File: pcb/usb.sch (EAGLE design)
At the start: 23 parts, among them CN2 JSTPH, Q1 mmbt2222, Q2 mmbt2222, Q3 DMG3415U, U2 MIC5225-3.3v, U4 CH340G, U6 MCP73831T-2ACI/OT

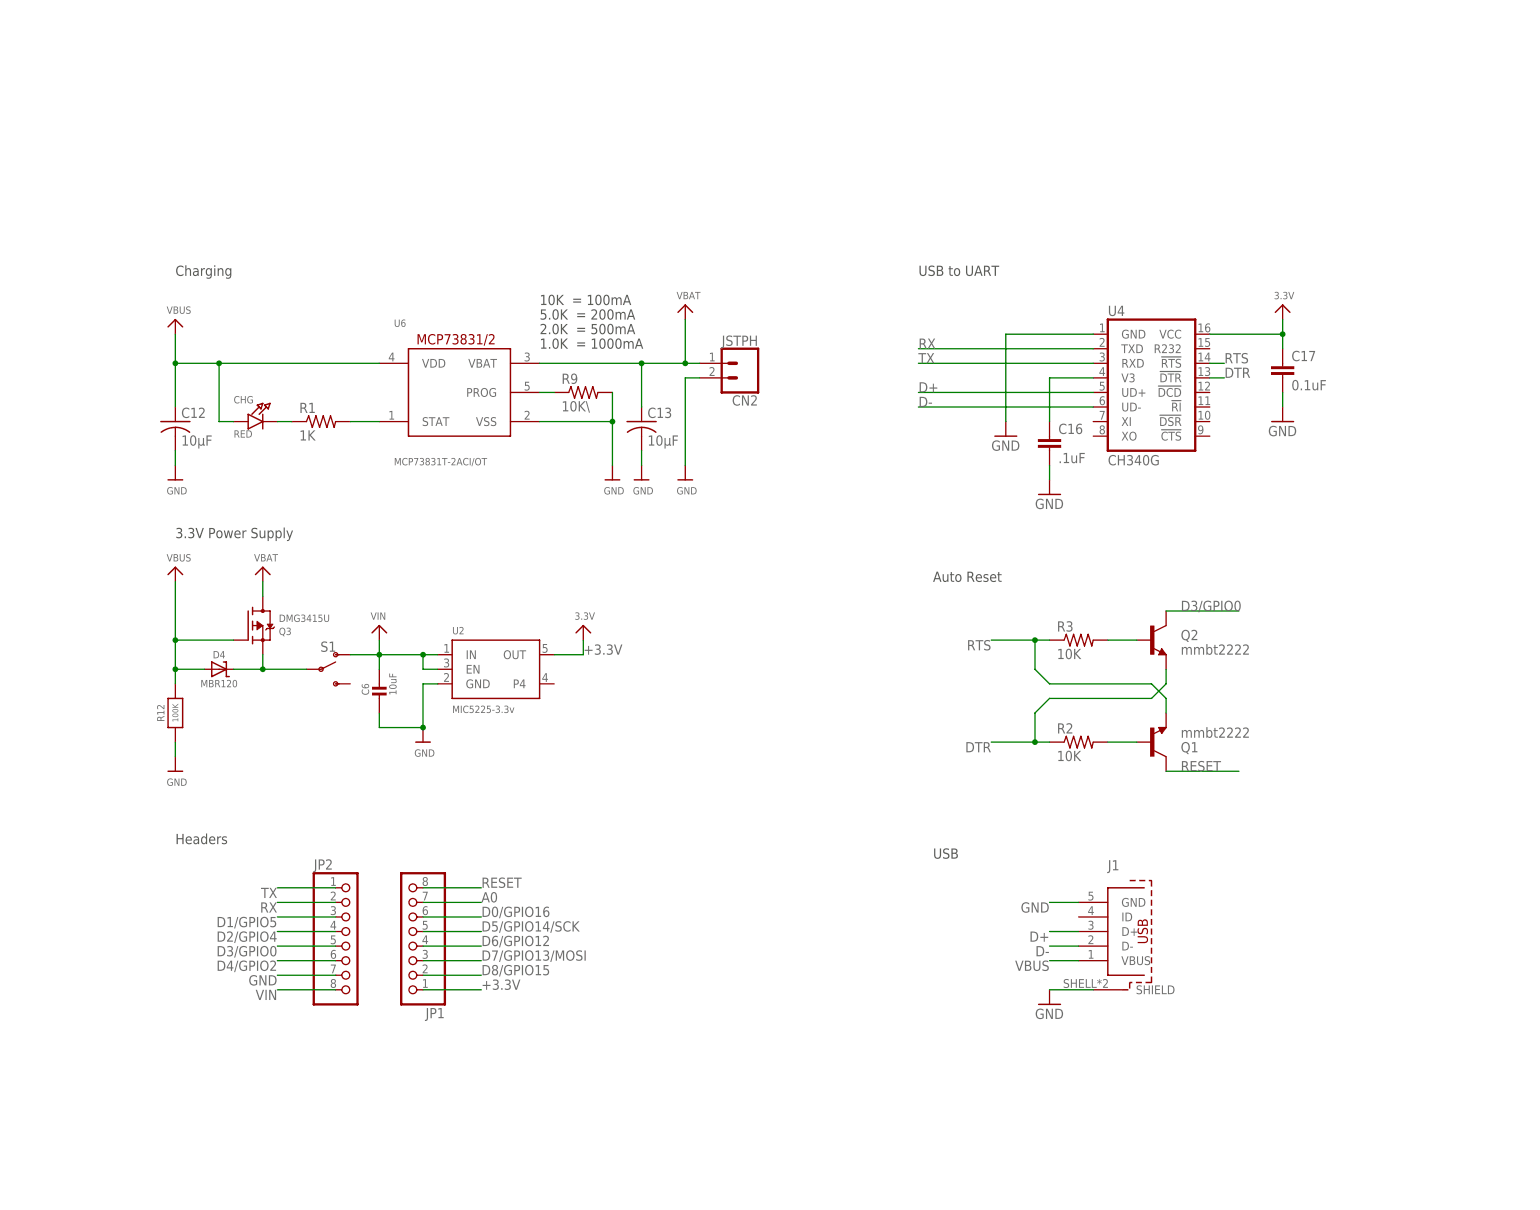
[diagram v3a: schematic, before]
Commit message: V2 usb board ordered
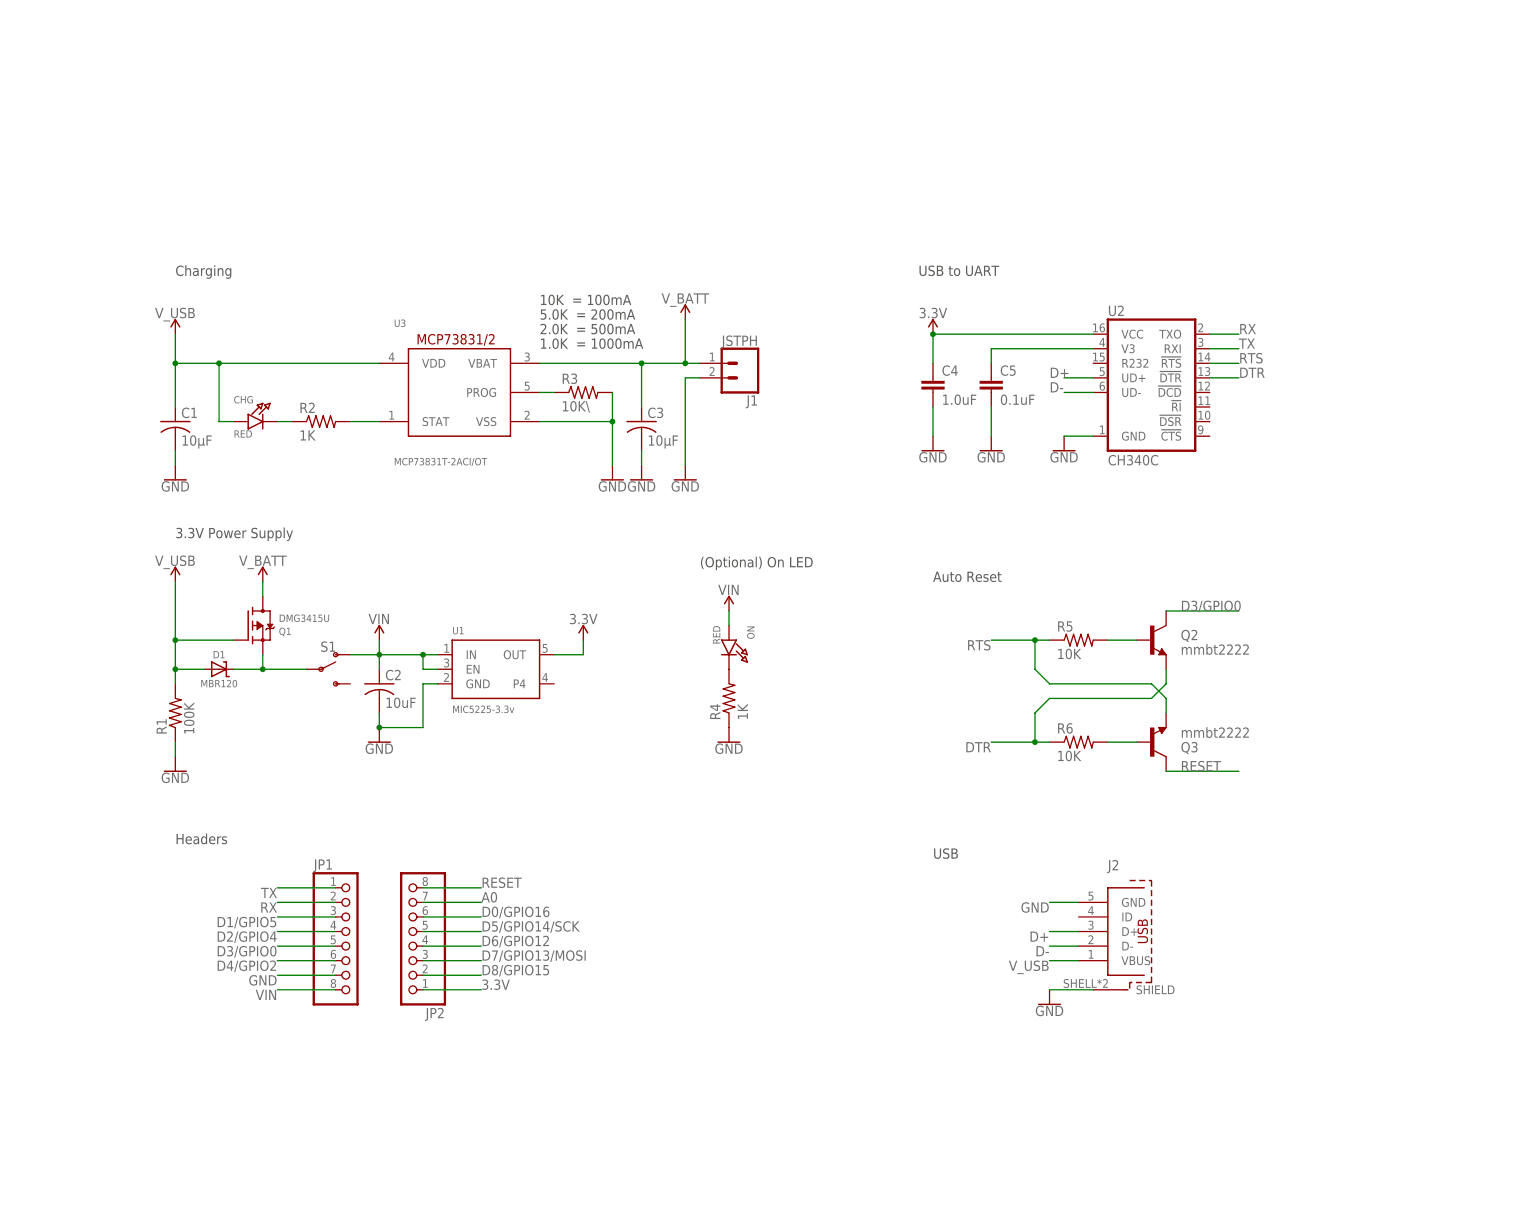
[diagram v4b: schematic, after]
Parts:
- removed C16: .1uF, SparkFun-Capacitors:10NF/10000PF-50V-10%(0603)
- removed C17: 0.1uF, SparkFun-Capacitors:0.1UF-25V(+80/-20%)(0603)
- removed C6: 10uF, microbuilder:CAP_CERAMIC0805
- removed CN2: JSTPH, SparkFun-Connectors:CONN_02
- removed R12: 100K, microbuilder:RESISTOR_0603_NOOUT
- removed R9: 10K\, adafruit:R-US_R0805
- removed U4: CH340G, SparkFun-DigitalIC:CH340GSMD
- added C2: 10uF, adafruit:C-USC0805
- added C4: 1.0uF, SparkFun-Capacitors:1.0UF-0805-25V-10%
- added C5: 0.1uF, SparkFun-Capacitors:1.0UF-0805-25V-10%
- added J2: (no value), Wurth_Elektronik_Electromechanic_Input-Output_Connectors_rev19b:614105150621
- added ON: RED, microbuilder:LED0805_NOOUTLINE
- added R4: 1K, adafruit:R-US_R0805
- added R5, R6: 10K, adafruit:R-US_R0603
- added U1: MIC5225-3.3v, microbuilder:VREG_SOT23-5
- J1: value (none) -> JSTPH; device Wurth_Elektronik_Electromechanic_Input-Output_Connectors_rev19a:614105150621 -> SparkFun-Connectors:CONN_02
- Q1: value mmbt2222 -> DMG3415U; device SparkFun:TRANSISTOR_NPNSOT23-3 -> microbuilder:MOSFET-P
- Q3: value DMG3415U -> mmbt2222; device microbuilder:MOSFET-P -> SparkFun:TRANSISTOR_NPNSOT23-3
- R1: value 1K -> 100K
- R2: value 10K -> 1K; device adafruit:R-US_R0603 -> adafruit:R-US_R0805
- R3: value 10K -> 10K\; device adafruit:R-US_R0603 -> adafruit:R-US_R0805
- U2: value MIC5225-3.3v -> CH340C; device microbuilder:VREG_SOT23-5 -> SparkFun-IC-Comms:CH340C
- renumbered C12 to C1, C13 to C3, D4 to D1, U6 to U3
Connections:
- removed net +3.3V: JP1.1, U2.OUT
- removed net V3: C16.1, U4.V3
- removed net VBAT: C3.1, CN2.1, Q3.D, U3.VBAT
- removed net VBUS: C1.1, CHG.A, D1.A, J1.VBUS, Q3.G, R12.2, U3.VDD
- new net N$2: C5.1, U2.V3
- new net N$3: ON.C, R4.2
- new net V_BATT: C3.1, J1.1, Q1.D, U3.VBAT
- new net V_USB: C1.1, CHG.A, D1.A, J2.VBUS, Q1.G, R1.2, U3.VDD
- net 3.3V: now also C4.1, JP2.1, U1.OUT, U2.VCC; no longer C17.1, U4.VCC
- net A0: now also JP2.7; no longer JP1.7
- net D+: now also J2.D+, U2.UD+; no longer J1.D+, U4.UD+
- net D-: now also J2.D-, U2.UD-; no longer J1.D-, U4.UD-
- net D0/GPIO16: now also JP2.6; no longer JP1.6
- net D1/GPIO5: now also JP1.3; no longer JP2.3
- net D2/GPIO4: now also JP1.4; no longer JP2.4
- net D3/GPIO0: now also JP1.5; no longer JP2.5
- net D4/GPIO2: now also JP1.6; no longer JP2.6
- net D5/GPIO14/SCK: now also JP2.5; no longer JP1.5
- net D6/GPIO12: now also JP2.4; no longer JP1.4
- net D7/GPIO13/MOSI: now also JP2.3; no longer JP1.3
- net D8/GPIO15: now also JP2.2; no longer JP1.2
- net DTR: now also R6.1, U2.!DTR; no longer R2.1, U4.!DTR
- net GND: now also C2.2, C4.2, C5.2, J1.2, J2.GND, J2.SHIELD, JP1.7, R1.1, R3.2, R4.1, U1.GND; no longer C16.2, C17.2, C6.P$2, CN2.2, J1.GND, J1.SHIELD, JP2.7, R12.1, R9.2, U4.GND
- net N$1: now also R2.1; no longer R1.1
- net N$13: now also Q3.B, R6.2; no longer Q1.B, R2.2
- net N$14: now also R5.2; no longer R3.2
- net N$4: now also R2.2; no longer R1.2
- net N$7: now also Q1.S; no longer Q3.S
- net N$9: now also R3.1; no longer R9.1
- net RESET: now also JP2.8, Q3.C; no longer JP1.8, Q1.C
- net RTS: now also Q3.E, R5.1, U2.!RTS; no longer Q1.E, R3.1, U4.!RTS
- net RX: now also JP1.2, U2.TXO; no longer JP2.2, U4.TXD
- net TX: now also JP1.1, U2.RXI; no longer JP2.1, U4.RXD
- net VIN: now also C2.1, JP1.8, ON.A, U1.EN, U1.IN; no longer C6.P$1, JP2.8, U2.EN, U2.IN
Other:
- note added: "(Optional) On LED"
- moved on the sheet: JP1, JP2, R1, R2, R3

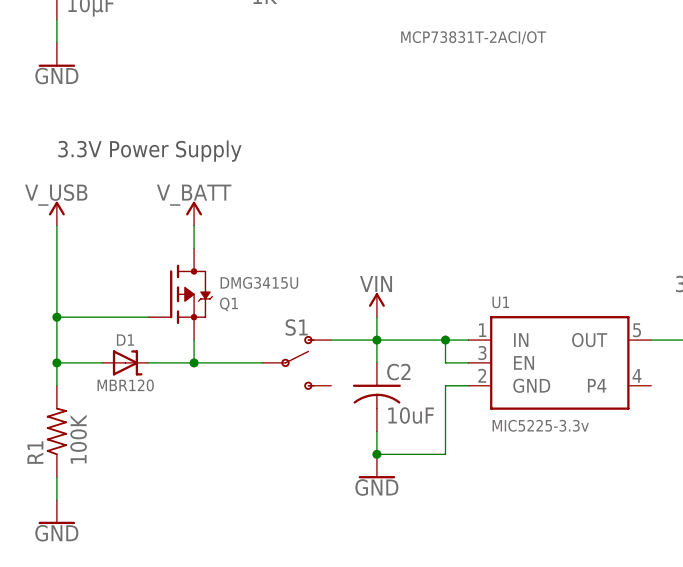
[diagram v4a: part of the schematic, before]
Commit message: Add manufacturer part numbers to USB board
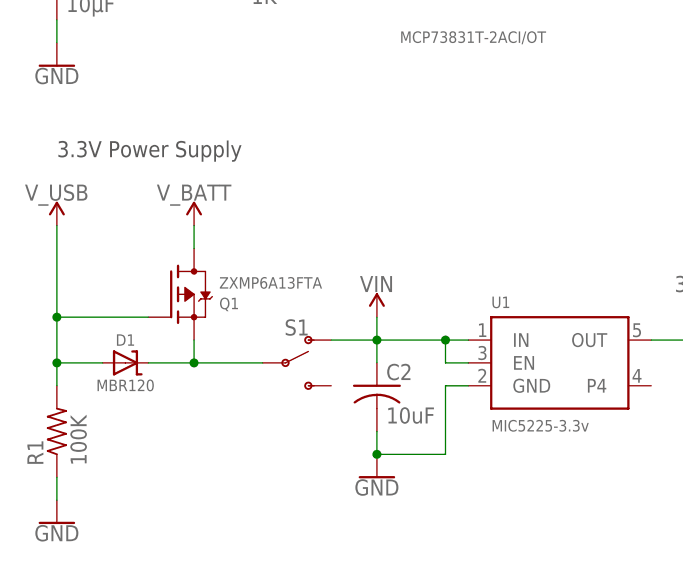
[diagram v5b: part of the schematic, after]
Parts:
- C1, C2, C3: MPN (none) -> EMK212ABJ106KG-T
- C4: MPN (none) -> C0805C105K4RAC7210
- C5: MPN (none) -> 08051C104J4T4A
- CHG: MPN (none) -> SMLD12E3N1WT86
- D1: MPN (none) -> MBR120ESFT1G
- J2: MPN (none) -> 614105150621
- ON: MPN (none) -> SMLEN3WBC8W1
- Q1: value DMG3415U -> ZXMP6A13FTA; MPN (none) -> ZXMP6A13FTA
- Q2, Q3: MPN (none) -> MMBT2222A-G
- R1: MPN (none) -> CR0805AFX-1003EAS
- R2, R4: MPN (none) -> ESR10EZPJ102
- R3, R5, R6: MPN (none) -> CRCW080510K0FKEAC
- S1: MPN (none) -> AYZ0202AGRLC
- U1: MPN (none) -> MIC5225-3.3YM5-TR
- U2: MPN (none) -> CH340C
- U3: MPN (none) -> MCP73831T-2ACI/OT

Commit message: Add part numbers for the headers on the usb board
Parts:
- JP1, JP2: MPN (none) -> 8Fx1L-254mm
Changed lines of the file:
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@@
 <attribute name="MPN" value="MMBT2222A-G"/>
 </part>
-<part name="JP2" library="adafruit" library_urn="urn:adsk.eagle:library:420" deviceset="PINHD-1X8" device="CLEANBIG" package3d_urn="urn:adsk.eagle:package:6240708/1"/>
-<part name="JP1" library="adafruit" library_urn="urn:adsk.eagle:library:420" deviceset="PINHD-1X8" device="CLEANBIG" package3d_urn="urn:adsk.eagle:package:6240708/1"/>
+<part name="JP2" library="adafruit" library_urn="urn:adsk.eagle:library:420" deviceset="PINHD-1X8" device="CLEANBIG" package3d_urn="urn:adsk.eagle:package:6240708/1">
+<attribute name="MPN" value="8Fx1L-254mm"/>
+</part>
+<part name="JP1" library="adafruit" library_urn="urn:adsk.eagle:library:420" deviceset="PINHD-1X8" device="CLEANBIG" package3d_urn="urn:adsk.eagle:package:6240708/1">
+<attribute name="MPN" value="8Fx1L-254mm"/>
+</part>
 <part name="J2" library="Wurth_Elektronik_Electromechanic_Input-Output_Connectors_rev19b" library_urn="urn:adsk.eagle:library:488835" deviceset="614105150621" device="" package3d_urn="urn:adsk.eagle:package:3360156/4">
 <attribute name="MPN" value="614105150621"/>
@@
 <attribute name="NAME" x="64.77" y="9.525" size="1.778" layer="95" rot="R180"/>
 <attribute name="VALUE" x="64.77" y="35.56" size="1.778" layer="96" rot="R180"/>
+<attribute name="MPN" x="58.42" y="20.32" size="1.778" layer="96" rot="R180" display="off"/>
 </instance>
 <instance part="JP1" gate="G$1" x="48.26" y="22.86" smashed="yes">
 <attribute name="NAME" x="41.91" y="33.655" size="1.778" layer="95"/>
 <attribute name="VALUE" x="41.91" y="7.62" size="1.778" layer="96"/>
+<attribute name="MPN" x="48.26" y="22.86" size="1.778" layer="96" display="off"/>
 </instance>
 <instance part="J2" gate="G$1" x="182.88" y="22.86" smashed="yes">

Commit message: Use cheaper 0.1uF capacitors and 10uF capacitors
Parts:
- C1, C2, C3: MPN EMK212ABJ106KG-T -> LMK212BJ106KG-T
- C5: MPN 08051C104J4T4A -> C0805C104M3RACTU
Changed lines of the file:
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@@
 <part name="J1" library="SparkFun-Connectors" library_urn="urn:adsk.eagle:library:513" deviceset="CONN_02" device="" package3d_urn="urn:adsk.eagle:package:38039/1" value="JSTPH"/>
 <part name="C1" library="adafruit" library_urn="urn:adsk.eagle:library:420" deviceset="C-US" device="C0805" package3d_urn="urn:adsk.eagle:package:6240337/1" value="10µF">
-<attribute name="MPN" value="EMK212ABJ106KG-T"/>
+<attribute name="MPN" value="LMK212BJ106KG-T"/>
 </part>
 <part name="C3" library="adafruit" library_urn="urn:adsk.eagle:library:420" deviceset="C-US" device="C0805" package3d_urn="urn:adsk.eagle:package:6240337/1" value="10µF">
-<attribute name="MPN" value="EMK212ABJ106KG-T"/>
+<attribute name="MPN" value="LMK212BJ106KG-T"/>
 </part>
 <part name="R3" library="adafruit" library_urn="urn:adsk.eagle:library:420" deviceset="R-US_" device="R0805" package3d_urn="urn:adsk.eagle:package:6240566/1" value="10K\">
@@
 </part>
 <part name="C5" library="SparkFun-Capacitors" library_urn="urn:adsk.eagle:library:510" deviceset="1.0UF" device="-0805-25V-10%" package3d_urn="urn:adsk.eagle:package:37429/1" value="0.1uF">
-<attribute name="MPN" value="08051C104J4T4A"/>
+<attribute name="MPN" value="C0805C104M3RACTU"/>
 </part>
 <part name="ON" library="microbuilder" deviceset="LED" device="0805_NOOUTLINE" value="RED">
@@
 <part name="GND11" library="SparkFun-PowerSymbols" library_urn="urn:adsk.eagle:library:530" deviceset="GND" device=""/>
 <part name="C2" library="adafruit" library_urn="urn:adsk.eagle:library:420" deviceset="C-US" device="C0805" package3d_urn="urn:adsk.eagle:package:6240337/1" value="10uF">
-<attribute name="MPN" value="EMK212ABJ106KG-T"/>
+<attribute name="MPN" value="LMK212BJ106KG-T"/>
 </part>
 </parts>
